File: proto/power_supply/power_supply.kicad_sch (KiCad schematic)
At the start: 35 parts, among them J101 Conn_01x02, J102 Conn_01x02, J103 Conn_01x02, U1 LDK130-33_SOT23_SOT353, U101 ZXCT1110, U103 LMR51430

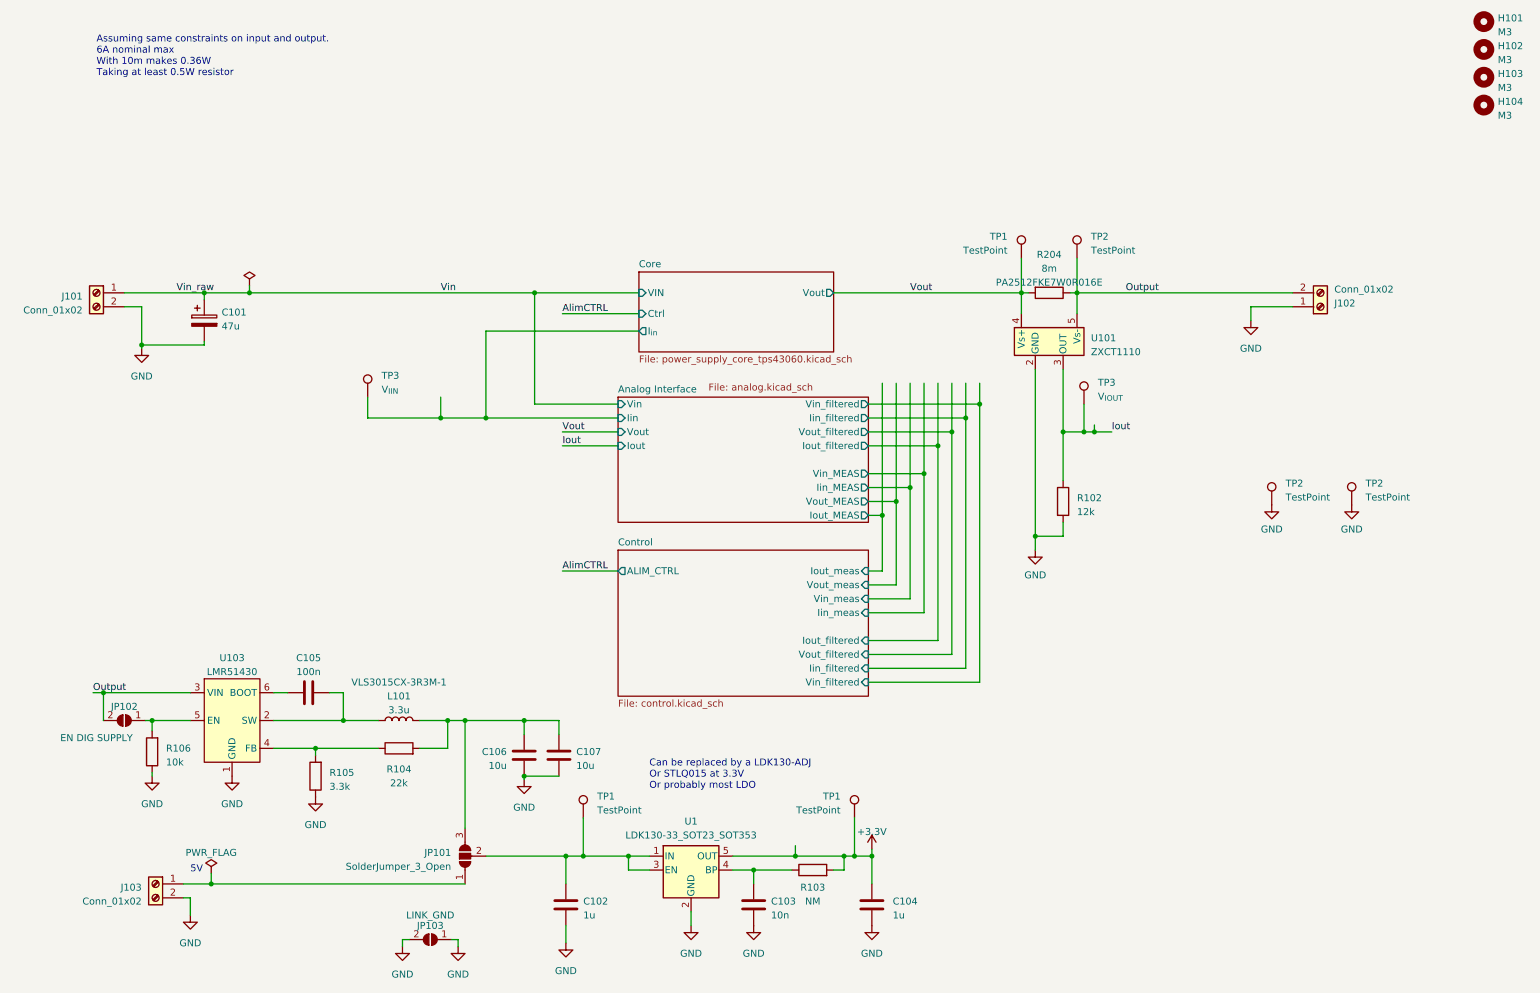
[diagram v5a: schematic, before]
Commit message: Update for BOM
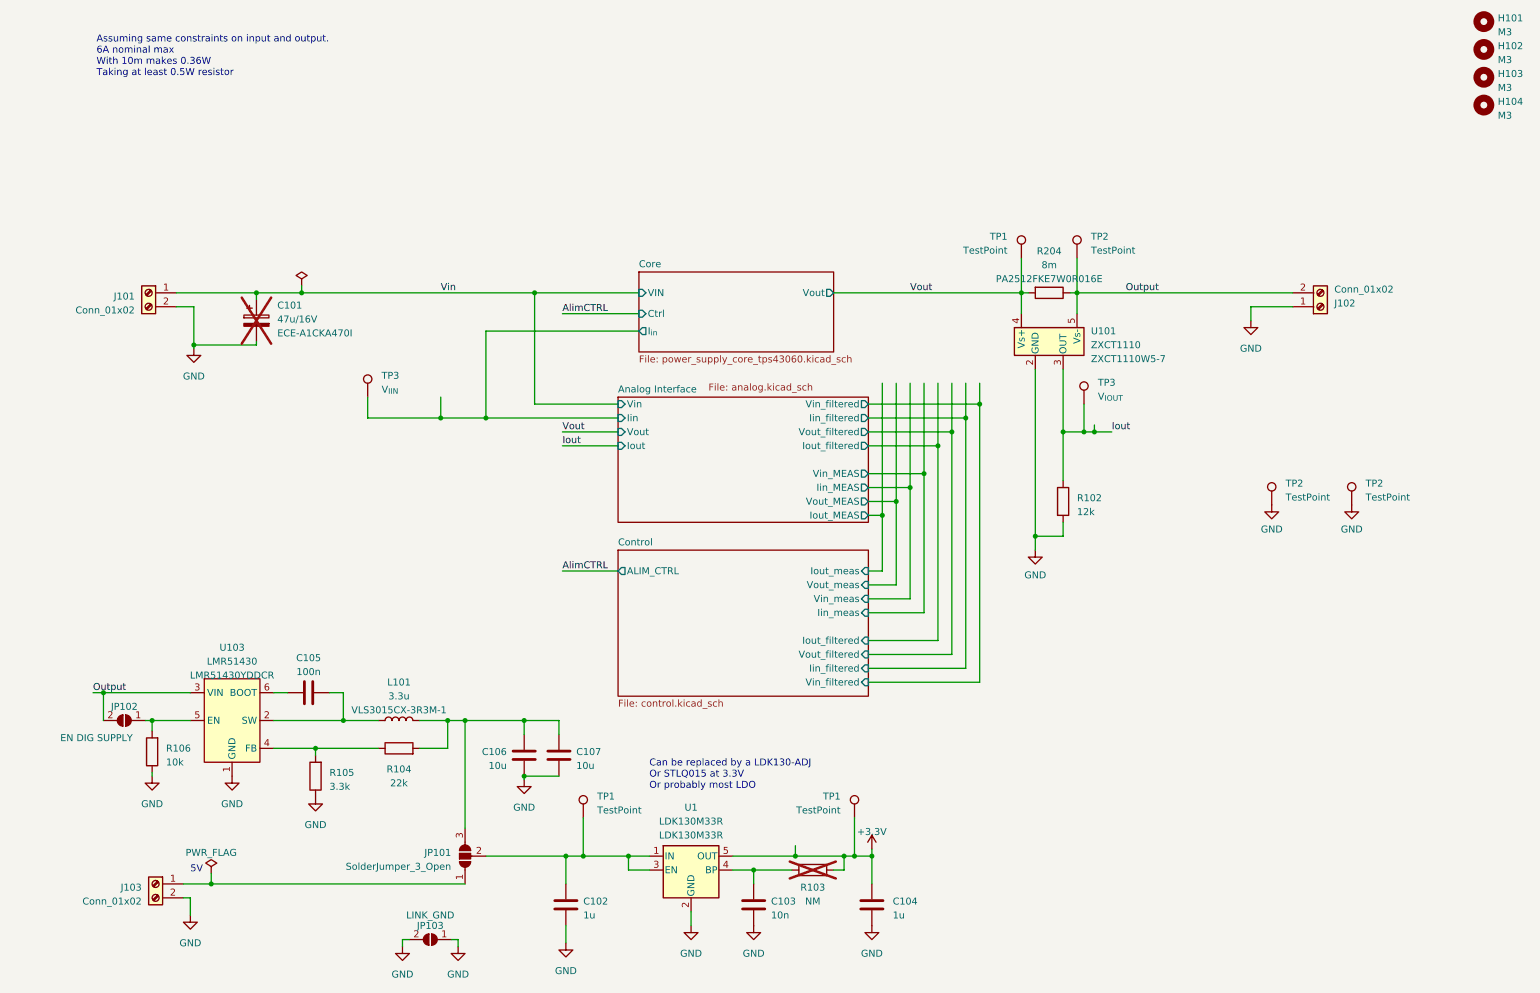
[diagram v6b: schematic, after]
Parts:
- C101: value 47u -> 47u/16V; MPN (none) -> ECE-A1CKA470I; now not fitted; now left out of the parts list
- H101, H102, H103, H104, JP101, JP102, JP103, TP1, TP2, TP3: now left out of the parts list
- R103: now not fitted; now left out of the parts list
- U1: value LDK130-33_SOT23_SOT353 -> LDK130M33R; MPN (none) -> LDK130M33R
- U101: MPN (none) -> ZXCT1110W5-7
- U103: MPN (none) -> LMR51430YDDCR
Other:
- company: (none) -> Julien FAUCHER
- title: (none) -> MPPT PSU - Top
- moved on the sheet: J101

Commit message: [PCB] Elaborate BOM
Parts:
- C101: Mouser SKU (none) -> 667-ECE-A1CKA470I
- C105: MPN (none) -> 0805YC104M4T2A; Mouser SKU (none) -> 581-0805YC104M4T2A
- J101, J102, J103: now left out of the parts list
- L101: Mouser SKU (none) -> 810-VLS3015CX3R3M1
- R204: Mouser SKU (none) -> 603-PA2512FKE7W0R16E
- U1: Mouser SKU (none) -> 511-LDK130M33R
- U101: Mouser SKU (none) -> 522-ZXCT1110W5-7
- U103: Mouser SKU (none) -> 595-LMR51430YDDCR

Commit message: Start overall new board
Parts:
- R104: value 22k -> 150k
- R105: value 3.3k -> 20k
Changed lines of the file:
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@@
-(kicad_sch (version 20230221) (generator eeschema)
+(kicad_sch (version 20230409) (generator eeschema)
   (paper "A4")
   (title_block
@@
     (stroke (width 0) (type default))
   )
-  (text "Assuming same constraints on input and output.\n6A nominal max\nWith 10m makes 0.36W \nTaking at least 0.5W resistor"
+  (text "Assuming same constraints on input and output.\n6A nominal max\nWith 10m makes 0.36W \nTaking at least 0.5W resistor" (exclude_from_sim no)
     (at 19.05 26.67 0)
     (effects (font (size 1.27 1.27)) (justify left bottom))
   )
-  (text "5V" (at 36.195 172.085 0)
-    (effects (font (size 1.27 1.27)) (justify left bottom))
-  )
-  (text "Can be replaced by a LDK130-ADJ\nOr STLQ015 at 3.3V\nOr probably most LDO"
+  (text "5V" (exclude_from_sim no)
+ (at 36.195 172.085 0)
+    (effects (font (size 1.27 1.27)) (justify left bottom))
+  )
+  (text "Can be replaced by a LDK130-ADJ\nOr STLQ015 at 3.3V\nOr probably most LDO" (exclude_from_sim no)
     (at 120.015 156.845 0)
     (effects (font (size 1.27 1.27)) (justify left bottom))
@@
   (symbol (lib_id "Device:R") (at 59.055 154.305 180) (unit 1)
     (in_bom yes) (on_board yes) (dnp no) (fields_autoplaced)
-    (property "Reference" "R105" (at 61.595 153.67 0)
+    (property "Reference" "R105" (at 60.96 153.67 0)
       (effects (font (size 1.27 1.27)) (justify right))
     )
-    (property "Value" "3.3k" (at 61.595 156.21 0)
+    (property "Value" "20k" (at 60.96 156.21 0)
       (effects (font (size 1.27 1.27)) (justify right))
     )
@@
   (symbol (lib_id "Device:R") (at 74.295 149.225 90) (unit 1)
     (in_bom yes) (on_board yes) (dnp no) (fields_autoplaced)
-    (property "Reference" "R104" (at 74.295 153.035 90)
-      (effects (font (size 1.27 1.27)))
-    )
-    (property "Value" "22k" (at 74.295 155.575 90)
-      (effects (font (size 1.27 1.27)))
-    )
+    (property "Reference" "R104" (at 74.295 152.4 90)
+      (effects (font (size 1.27 1.27)))
+    )
+    (property "Value" "150k" (at 74.295 154.94 90)
+      (effects (font (size 1.27 1.27)))
+    )
